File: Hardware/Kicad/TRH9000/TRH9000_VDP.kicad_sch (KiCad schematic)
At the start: 13 parts, among them U1 V9990, U2 KM428C256, U3 KM428C256, X1 Crystek_CE3291, Y1 21.47727Mhz

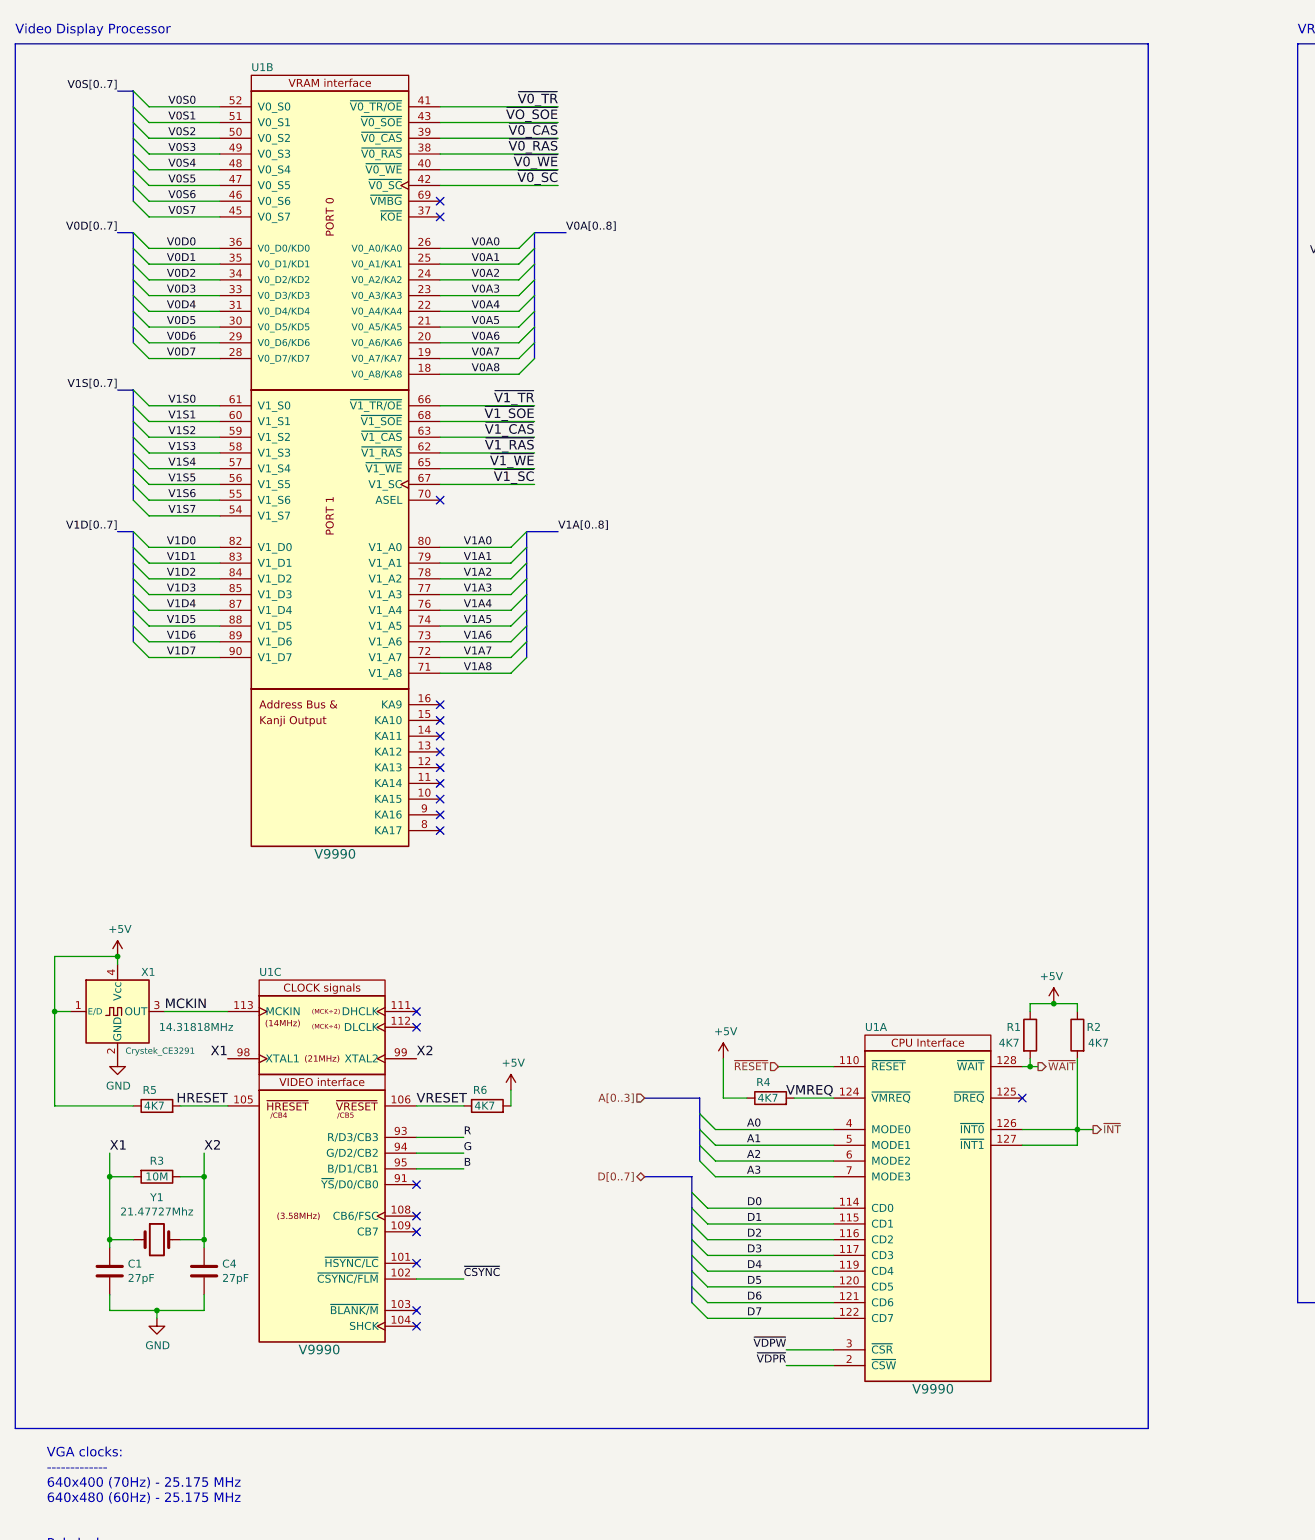
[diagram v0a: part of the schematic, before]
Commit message: Started routing the PCB, adding cut-outs to separate the analog from digital signal-domains.
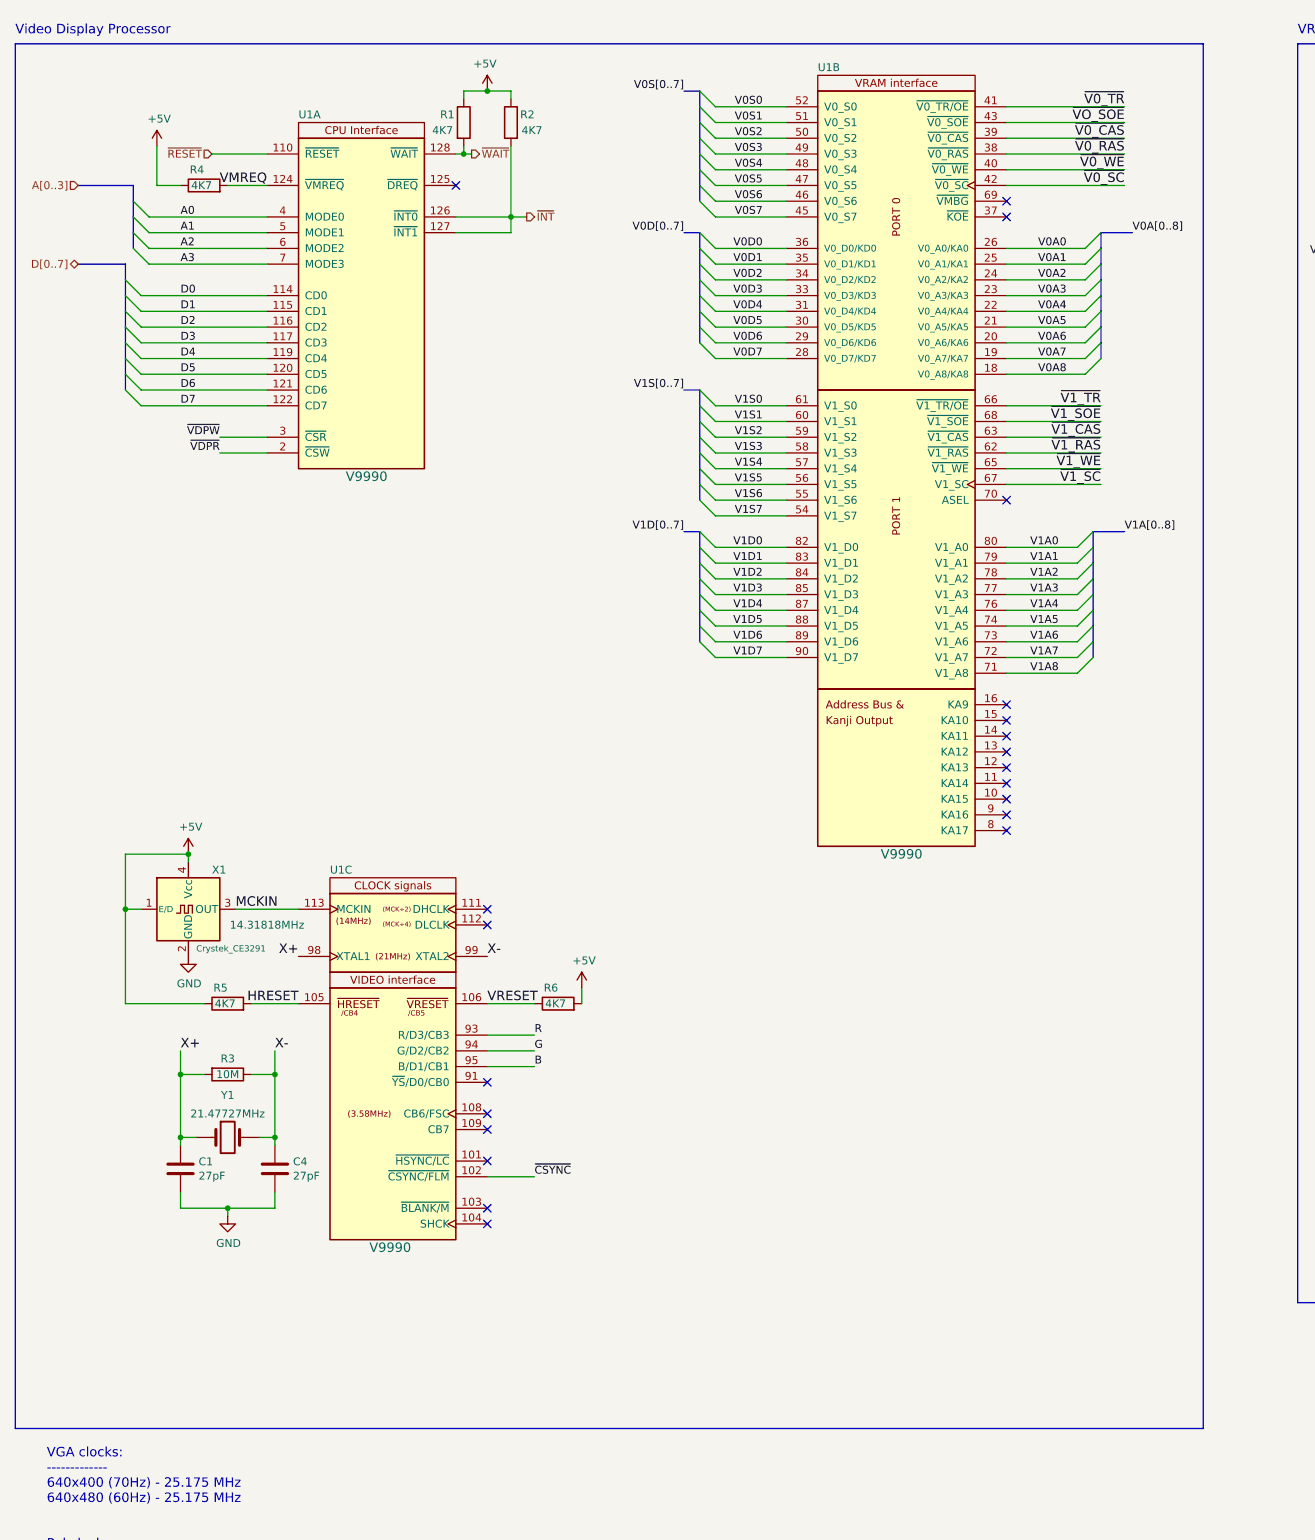
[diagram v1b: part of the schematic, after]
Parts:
- Y1: value 21.47727Mhz -> Y_HCM4921477270ABJT; footprint Crystal:Crystal_HC49-U_Vertical -> LRJ:Crystal_HC49-US_Vertical; symbol Device:Crystal -> LRJ-parts:Y_HCM4921477270ABJT; Frequency (none) -> 21.47727MHz; Manufacturer (none) -> Citizen Finedevice Co Ltd; Status (none) -> Active
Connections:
- net X1 renamed X+
- net X2 renamed X-
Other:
- moved on the sheet: C1, C4, R1, R2, R3, R4, R5, R6, U1A, U1B, U1C, X1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

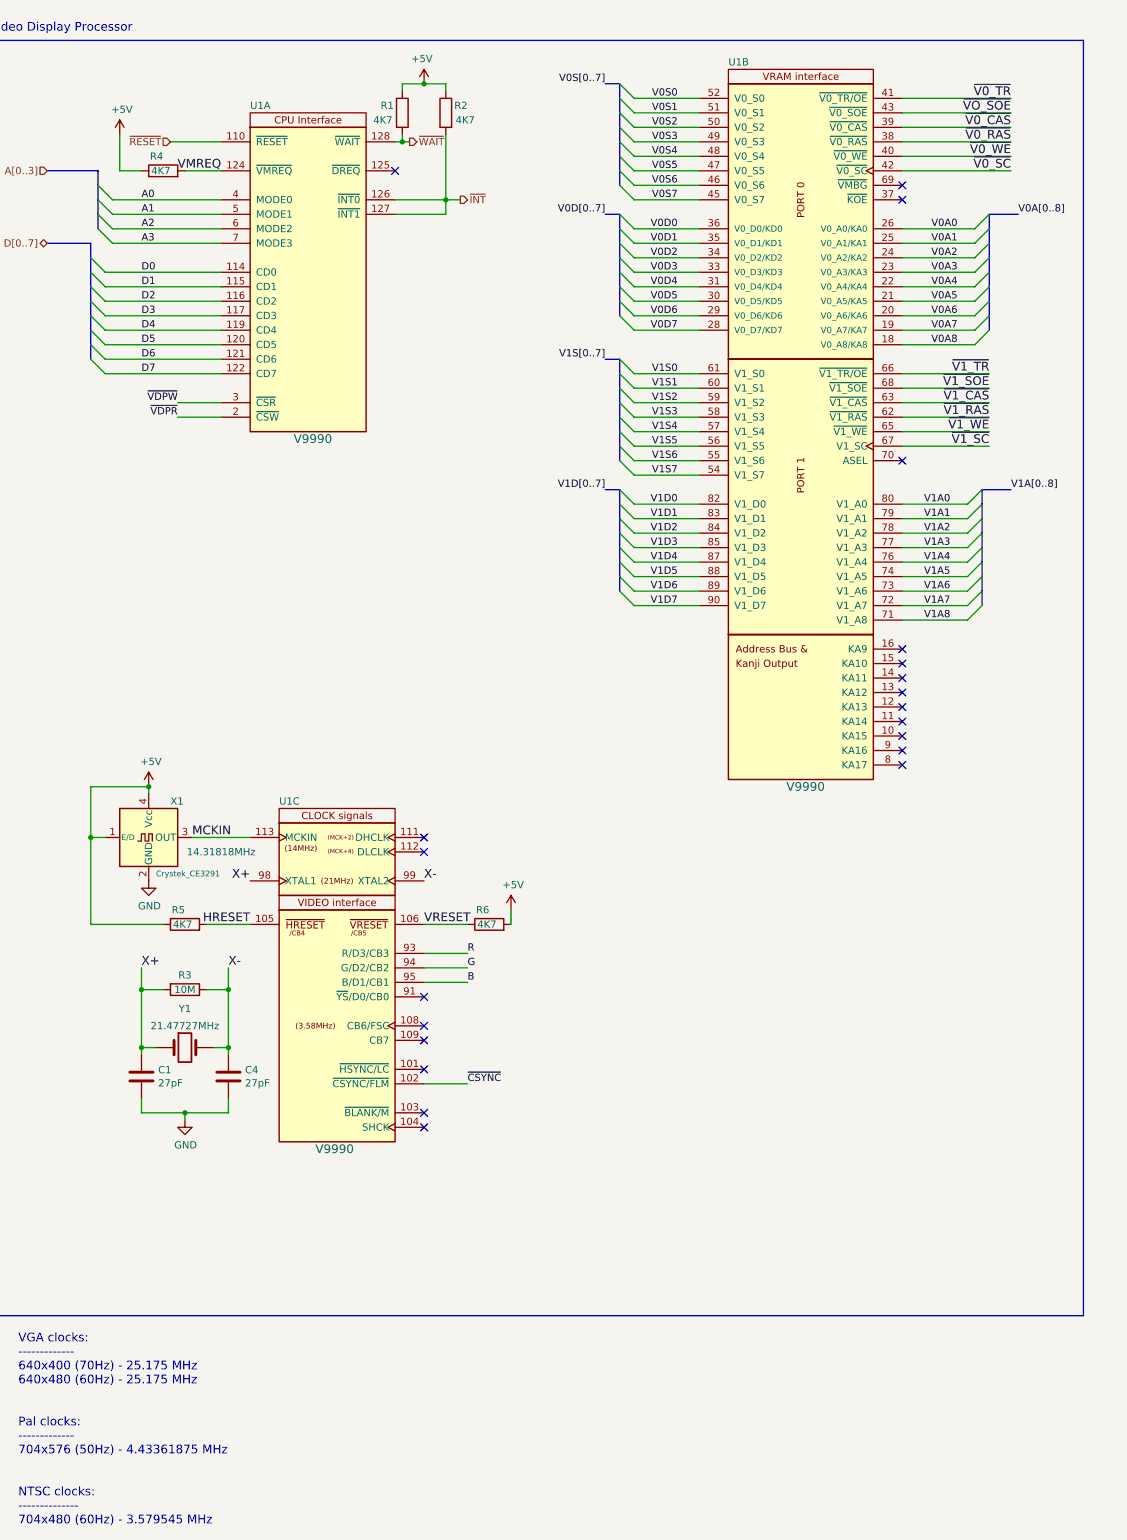
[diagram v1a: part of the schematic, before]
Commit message: More routing of the analog portion. Added 3D-models for the VGA and Scart connectors.
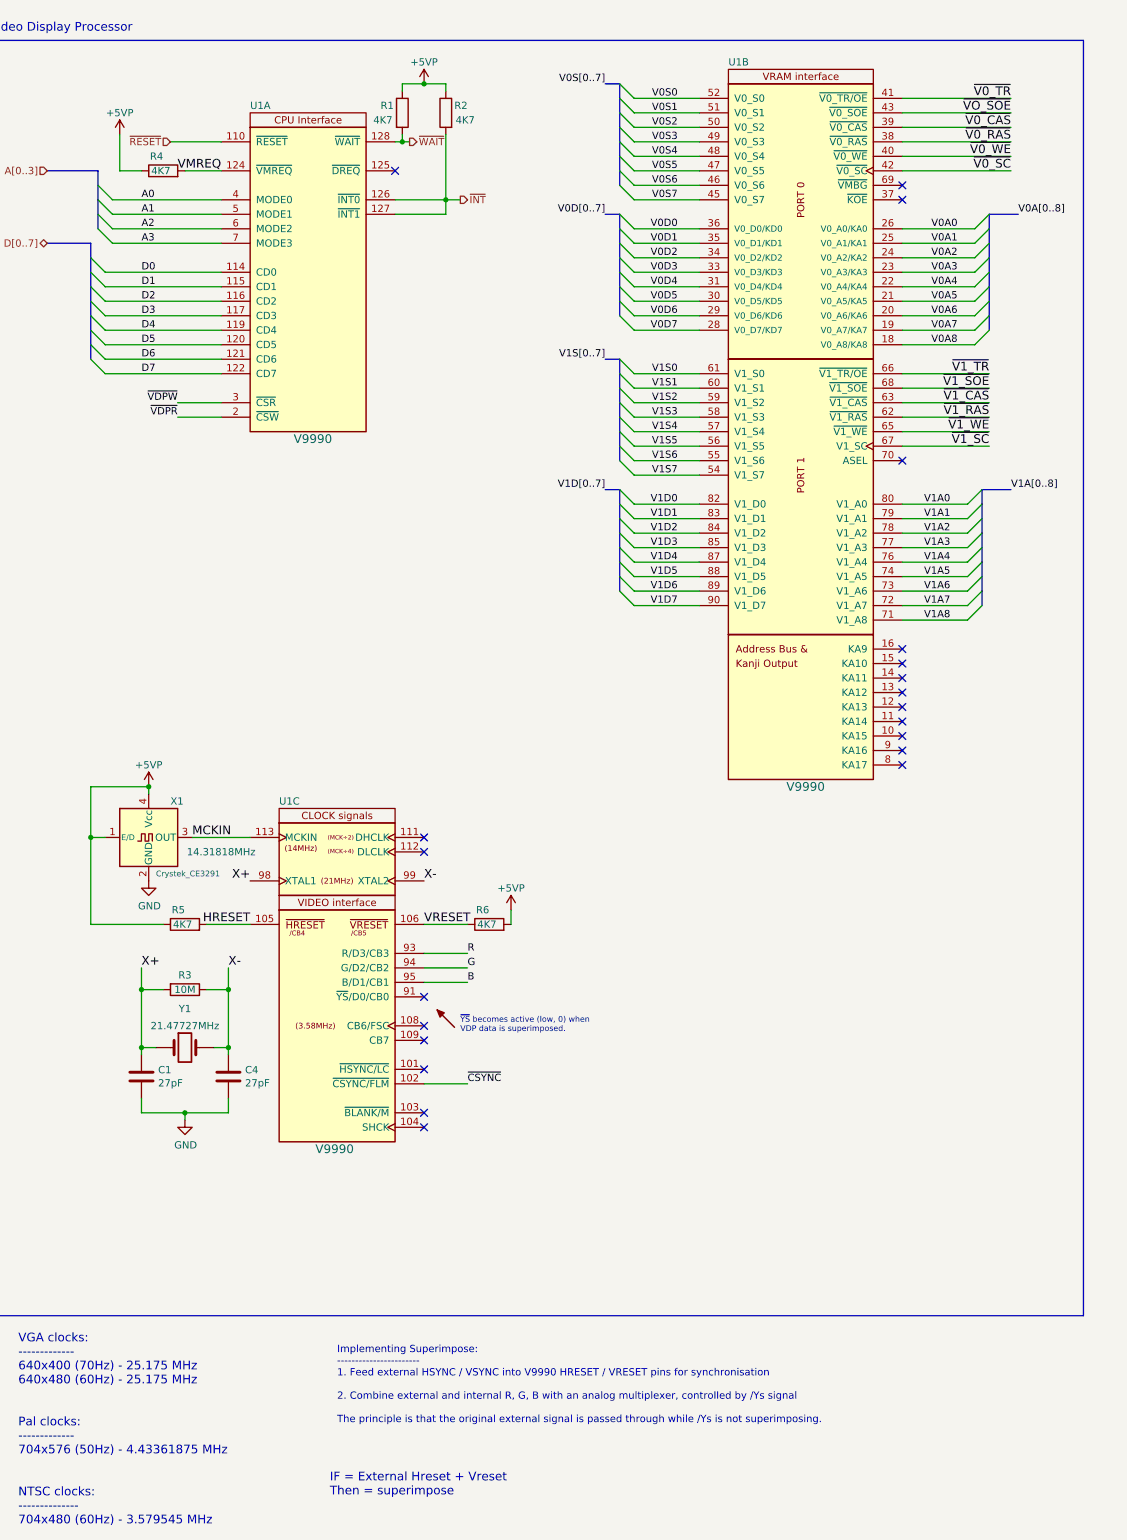
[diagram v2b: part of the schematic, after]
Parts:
- U1: Status (none) -> OBSOLETE
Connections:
- net +5V renamed +5VP
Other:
- note added: "IF = External Hreset + Vreset Then = superimpose"
- note added: "Implementing Superimpose: ----------------------- 1. Feed external HSYNC / VSYNC into V9990 HRESET / VRESET pins for synchronisation 2. Combine external and internal R, G, B with an analog multiplexer, controlled by /Ys signal The principle is that the original external signal is passed through while /Ys is not superimposing."
- note added: "~{YS} becomes active (low, 0) when VDP data is superimposed."

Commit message: Did a reroute of the analog / digital separation.
Did a reroute of the analog / digital separation.
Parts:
- added R34: 4K7, Resistor_SMD:R_0805_2012Metric, symbol Device:R
- added U9: SST39SF010A-lrj, Package_SO:TSOP-I-32_12.4x8mm_P0.5mm, symbol LRJ-parts:SST39SF010A-lrj
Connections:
- net +5VP: now also R34.1; no longer R5.1, R6.2, X1.1 (E/D), X1.4 (Vcc)
- net V0A0: now also U9.20 (A0)
- net V0A1: now also U9.19 (A1)
- net V0A2: now also U9.18 (A2)
- net V0A3: now also U9.17 (A3)
- net V0A4: now also U9.16 (A4)
- net V0A5: now also U9.15 (A5)
- net V0A6: now also U9.14 (A6)
- net V0A7: now also U9.13 (A7)
- net V0A8: now also U9.3 (A8)
- net V0D0: now also U9.21 (DQ0)
- net V0D1: now also U9.22 (DQ1)
- net V0D2: now also U9.23 (DQ2)
- net V0D3: now also U9.25 (DQ3)
- net V0D4: now also U9.26 (DQ4)
- net V0D5: now also U9.27 (DQ5)
- net V0D6: now also U9.28 (DQ6)
- net V0D7: now also U9.29 (DQ7)
- net ~{YSi}: now reaches U1.91 (~{YS}/D0/CB0)
- net KA15: now reaches U1.10 (KA15)
- net KA15: now also U9.11 (A15)
- net KA14: now reaches U1.11 (KA14)
- net KA14: now also U9.5 (A14)
- net KA13: now reaches U1.12 (KA13)
- net KA13: now also U9.4 (A13)
- net KA12: now reaches U1.13 (KA12)
- net KA12: now also U9.12 (A12)
- net KA11: now reaches U1.14 (KA11)
- net KA11: now also U9.1 (A11)
- net KA10: now reaches U1.15 (KA10)
- net KA10: now also U9.31 (A10)
- net KA9: now reaches U1.16 (KA9)
- net KA9: now also U9.2 (A9)
- net ~{KOE}: now reaches U1.37 (~{KOE})
- net ~{KOE}: now also U9.30 (~{CE}), U9.32 (~{OE})
- net KA16: now reaches U1.9 (KA16)
- net KA16: now also U9.10 (A16)
- net B renamed Bi
- net G renamed Gi
- net HRESET renamed V9958_HSYNC
- net R renamed Ri
- net VRESET renamed V9958_VSYNC
- net ~{CSYNC} renamed ~{CSYNCi}
- new net +5VA: R5.1, R6.2, X1.1 (E/D), X1.4 (Vcc)
- new net ~{KWE}: R34.2, U9.7 (~{WE})
- no-connect marks 23 -> 13
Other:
- note added: "KANJI ROM (optional)"
- note added: "Kanji Rom specs: -------------- Pins: ~{OE} 18 Address 8 Data 27 pin minimum"
- note added: "LEGEND: ------ VDP = Video Display Processor CLK = Clock CS = Chip Select SYS_CLK = MSX System Clock Ri, Gi, Bi = RGB Internal"
- note removed: "Implementing Superimpose: ----------------------- 1. Feed external HSYNC / VSYNC into V9990 HRESET / VRESET pins for synchronisation 2. Combine external and internal R, G, B with an analog multiplexer, controlled by /Ys signal The principle is that the original external signal is passed through while /Ys is not superimposing."
- moved on the sheet: C1, C4, R3, R5, R6, U1B, U1C, U2A, U3A, X1, Y1

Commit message: More routing - almost finished - only 29 more lines to go...
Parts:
- Y1: footprint LRJ:Crystal_HC49-US_Vertical -> trh9000:Crystal_HC49-US_Vertical_cy_mod
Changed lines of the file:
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@@
   (symbol (lib_id "power:+5VA") (at 101.6 162.56 0) (unit 1)
     (in_bom yes) (on_board yes)
-    (property "Reference" "#PWR?" (id 0) (at 101.6 166.37 0)
+    (property "Reference" "#PWR0110" (id 0) (at 101.6 166.37 0)
       (effects (font (size 1.27 1.27)) hide)
     )
@@
   (symbol (lib_id "power:+5VA") (at 36.83 162.56 0) (unit 1)
     (in_bom yes) (on_board yes)
-    (property "Reference" "#PWR?" (id 0) (at 36.83 166.37 0)
+    (property "Reference" "#PWR0111" (id 0) (at 36.83 166.37 0)
       (effects (font (size 1.27 1.27)) hide)
     )
@@
       (effects (font (size 1.27 1.27)) hide)
     )
-    (property "Footprint" "LRJ:Crystal_HC49-US_Vertical" (id 2) (at 49.53 219.71 0)
+    (property "Footprint" "trh9000:Crystal_HC49-US_Vertical_cy_mod" (id 2) (at 49.53 219.71 0)
       (effects (font (size 1.27 1.27)) hide)
     )
